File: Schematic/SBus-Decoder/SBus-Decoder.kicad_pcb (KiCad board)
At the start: 2 copper layers, 10 parts, among them J1 Conn_01x03_Male, J2 Conn_01x01_Male, J3 Conn_02x03_Odd_Even, U1 PIC16F18313-I_SN, U2 MCP1703A-3302_SOT23

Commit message: Initial pcb
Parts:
- moved C3 6.25 mm to (109.8, 105.8), turned to 180 degrees
- moved U1 5.15 mm to (115.5, 108.2)
- moved C2 5.03 mm to (115.2, 104.2)
- moved R1 4.27 mm to (117.8, 112.8), turned to 0 degrees
- moved J2 3.89 mm to (109.8, 113.2)
- moved U2 3.34 mm to (107.5, 108.8)
- moved C1 3.01 mm to (106.8, 112.8), turned to 270 degrees
- moved D1 2.36 mm to (114.0, 112.8), turned to 0 degrees
- moved J3 1.25 mm to (121.8, 106.5)
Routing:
- net VBUS: track 0.00 -> 29.1 mm
- net +3V3: track 0.00 -> 20.1 mm
- net GND: track 0.00 -> 16.0 mm, vias 0 -> 3
- net Net-(J1-Pad1): track 0.00 -> 12.7 mm
- net Net-(J3-Pad2): track 0.00 -> 7.25 mm
- net Net-(J3-Pad1): track 0.00 -> 4.06 mm
- net Net-(R1-Pad2): track 0.00 -> 2.77 mm
- net Net-(D1-Pad2): track 0.00 -> 2.14 mm
- net Net-(U1-Pad2): track 0.00 -> 1.27 mm
- added copper zone on B.Cu, net GND
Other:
- board outline added: 28.5 x 13.5 mm
- net class Power: trace_width 1 -> 0.5
- board text added: "S1"
- board text added: "S2"

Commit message: Schematic and pcb
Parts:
- added J4: TSW-104-08-G-T-RA, SamacSys_Parts:HDRRA12W64P254_3X4_1016X254X810P, F.Cu at (121.5, 106.0)
- J1: footprint Connector_Wire:SolderWire-0.75sqmm_1x03_P4.8mm_D1.25mm_OD2.3mm -> Connector_Wire:SolderWire-0.5sqmm_1x03_P4.6mm_D0.9mm_OD2.1mm
- J3: value Conn_02x03_Odd_Even -> Conn_01x01_Male; footprint Connector_PinHeader_2.54mm:PinHeader_2x03_P2.54mm_Horizontal -> Connector_PinHeader_2.54mm:PinHeader_1x01_P2.54mm_Vertical
- U1: value PIC16F18313-I_SN -> PIC18F04Q40-I_ST; footprint PIC16F18313:PIC16F18313-I&slash_SN -> PIC18F0xQ40:PIC18F04Q40-I&slash_ST
- moved J3 11.0 mm to (113.2, 113.5)
- moved D1 2.02 mm to (116.0, 113.0), turned to 270 degrees
- moved C2 1.03 mm to (114.2, 104.5)
- moved R1 0.56 mm to (118.2, 113.0), turned to 90 degrees
- moved U2 0.56 mm to (107.0, 109.0)
- moved C3 0.50 mm to (109.8, 106.2)
- moved J2 0.35 mm to (109.5, 113.5)
- moved J1 0.25 mm to (102.5, 104.2)
- moved U1 0.25 mm to (115.2, 108.2)
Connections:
- U1 pad 3: Net-(U1-Pad2) -> Net-(U1-Pad3)
- U1 pad 4: Net-(J1-Pad1) -> Net-(J3-Pad1)
- U1 pad 5: Net-(R1-Pad2) -> Net-(U1-Pad5)
- U1 pad 6: Net-(J3-Pad2) -> Net-(U1-Pad6)
- U1 pad 7: Net-(J3-Pad1) -> Net-(J1-Pad1)
- U1 pad 8: GND -> Net-(R1-Pad2)
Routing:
- net GND: track 16.0 -> 53.4 mm, vias 3 -> 4
- net VBUS: track 29.1 -> 40.2 mm
- net Net-(J3-Pad2): track 7.25 -> 0.00 mm
- net Net-(J4-Pad10): track 0.00 -> 5.99 mm
- net +3V3: track 20.1 -> 14.9 mm, vias 0 -> 1
- net Net-(J4-Pad7): track 0.00 -> 4.25 mm
- net Net-(J3-Pad1): track 4.06 -> 8.02 mm
- net Net-(J4-Pad1): track 0.00 -> 3.74 mm
- net Net-(J4-Pad4): track 0.00 -> 3.74 mm
- net Net-(U1-Pad2): track 1.27 -> 0.00 mm
- net Net-(R1-Pad2): track 2.77 -> 2.02 mm
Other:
- board size 28.5 x 13.5 mm -> 28.5 x 14.8 mm
- board text added: "*"
- board text added: "+"
- board text added: "-"
- board text added: "SBus Decoder V1.0 QES 2021"
- board text removed: "S1"
- board text removed: "S2"

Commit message: Single pcb layout complete
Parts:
- moved C1 72.3 mm to (56.8, 60.5)
- moved C2 72.3 mm to (64.2, 52.2)
- moved C3 72.3 mm to (59.8, 54.0)
- moved D1 72.3 mm to (66.0, 60.8)
- moved J2 72.3 mm to (59.5, 61.2)
- moved J3 72.3 mm to (63.2, 61.2)
- moved J4 72.3 mm to (71.5, 53.8)
- moved R1 72.3 mm to (68.2, 60.8)
- moved U1 72.3 mm to (65.2, 56.0)
- moved U2 72.3 mm to (57.0, 56.8)
- moved J1 71.9 mm to (52.5, 52.6)
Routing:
- net VBUS: track 40.2 -> 41.0 mm
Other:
- board size 28.5 x 14.8 mm -> 28.8 x 15.2 mm
- rule pad_to_mask_clearance: 0 -> 0.05

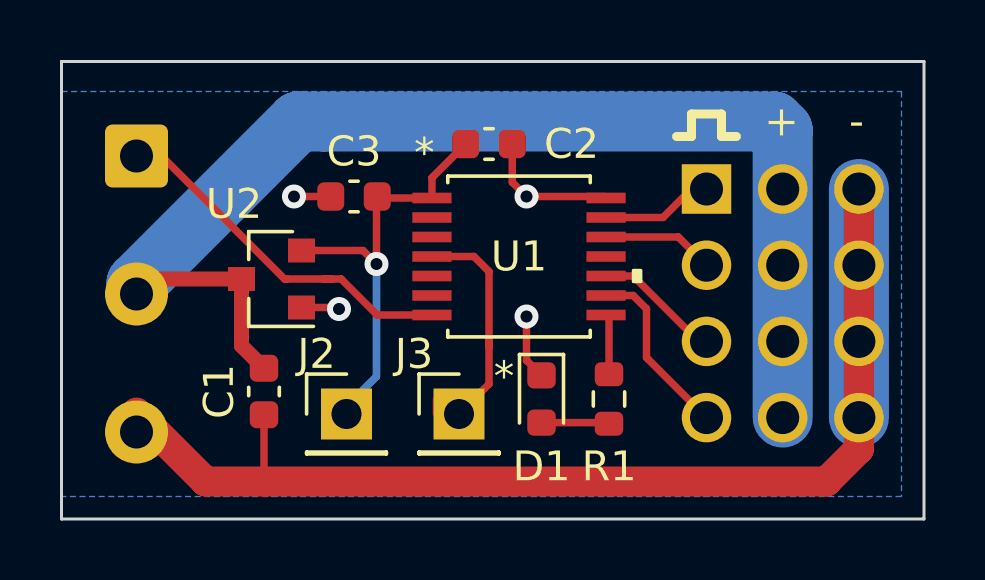
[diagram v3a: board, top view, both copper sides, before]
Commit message: Changed input connector footprint
Using a 2.54 pin header will allow for more flexibility for other uses (like a servo sequencer.)
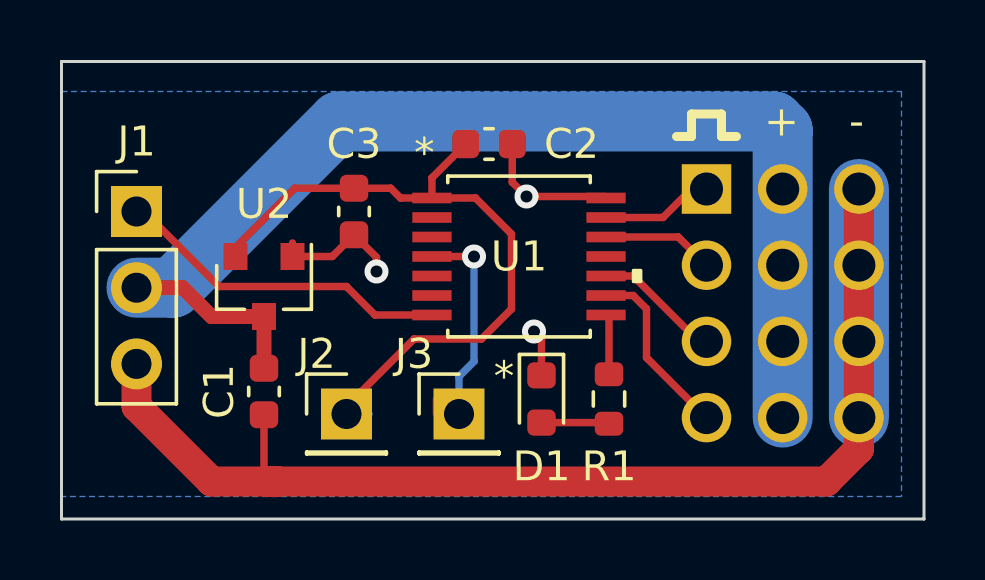
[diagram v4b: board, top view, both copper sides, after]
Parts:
- J1: footprint Connector_Wire:SolderWire-0.5sqmm_1x03_P4.6mm_D0.9mm_OD2.1mm -> Connector_PinHeader_2.54mm:PinHeader_1x03_P2.54mm_Vertical
- moved J1 1.85 mm to (52.5, 54.5), turned to 0 degrees
- moved C3 0.50 mm to (59.8, 54.5), turned to 270 degrees
- moved U2 0.35 mm to (56.8, 57.0), turned to 270 degrees
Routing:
- net +3V3: track 14.9 -> 23.8 mm, vias 1 -> 0
- net GND: track 53.4 -> 56.6 mm, vias 4 -> 3
- net Net-(J1-Pad1): track 12.8 -> 11.3 mm
- net Net-(J3-Pad1): track 8.02 -> 7.36 mm, vias 0 -> 1

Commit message: Better ICSP setup
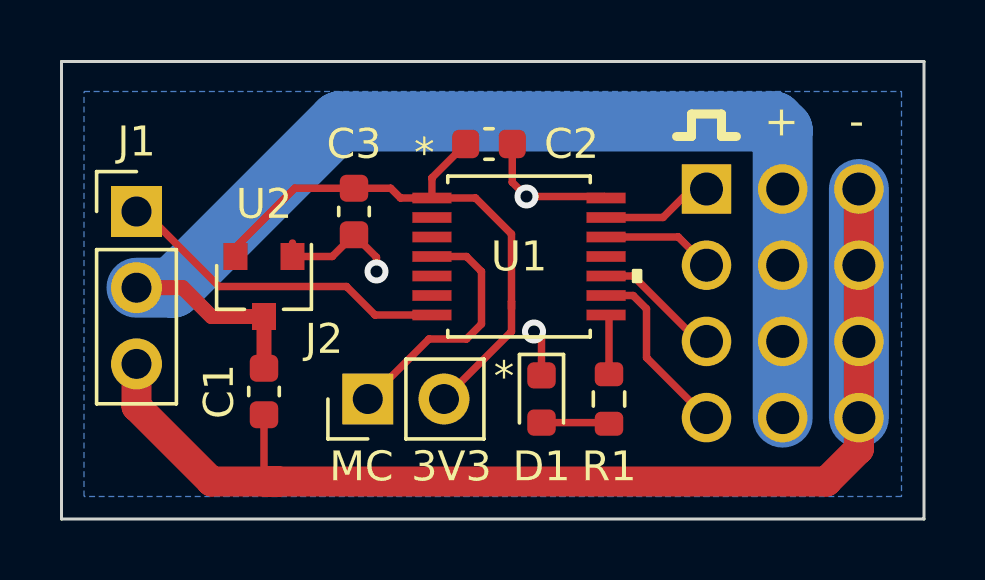
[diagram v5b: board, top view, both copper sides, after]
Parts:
- removed the J3 at (63.2, 61.2)
- C3: value 1 uF -> 2.2 uF
- J2: value Conn_01x01_Male -> Conn_01x02_Male; footprint Connector_PinHeader_2.54mm:PinHeader_1x01_P2.54mm_Vertical -> Connector_PinHeader_2.54mm:PinHeader_1x02_P2.54mm_Vertical
- moved J2 0.87 mm to (60.2, 60.8), turned to 90 degrees
- renumbered J4 to J3
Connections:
- J2 pad 1: +3V3 -> Net-(J2-Pad1)
- U1 pad 4: Net-(J3-Pad1) (its old number) -> Net-(J2-Pad1)
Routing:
- net Net-(J2-Pad1): track 0.00 -> 8.93 mm
- net Net-(J3-Pad1) (its old number): track 7.36 -> 0.00 mm, vias 1 -> 0
- net +3V3: track 23.8 -> 19.9 mm
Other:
- board text added: "3V3"
- board text added: "MC"

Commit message: Paneled and generated gerbers
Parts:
- added C1: 1 uF, Capacitor_SMD:C_0603_1608Metric, F.Cu at (112.2, 88.5)
- added C1: 1 uF, Capacitor_SMD:C_0603_1608Metric, F.Cu at (56.8, 102.5)
- added C1: 1 uF, Capacitor_SMD:C_0603_1608Metric, F.Cu at (56.8, 74.5)
- added C1: 1 uF, Capacitor_SMD:C_0603_1608Metric, F.Cu at (112.2, 102.5)
- added C1: 1 uF, Capacitor_SMD:C_0603_1608Metric, F.Cu at (112.2, 60.5)
- added C1: 1 uF, Capacitor_SMD:C_0603_1608Metric, F.Cu at (112.2, 74.5)
- added C1: 1 uF, Capacitor_SMD:C_0603_1608Metric, F.Cu at (84.5, 88.5)
- added C1: 1 uF, Capacitor_SMD:C_0603_1608Metric, F.Cu at (84.5, 102.5)
- added C1: 1 uF, Capacitor_SMD:C_0603_1608Metric, F.Cu at (84.5, 60.5)
- added C1: 1 uF, Capacitor_SMD:C_0603_1608Metric, F.Cu at (84.5, 74.5)
- added C1: 1 uF, Capacitor_SMD:C_0603_1608Metric, F.Cu at (56.8, 88.5)
- added C2: 0.1 uF, Capacitor_SMD:C_0603_1608Metric, F.Cu at (119.8, 80.2)
- added C2: 0.1 uF, Capacitor_SMD:C_0603_1608Metric, F.Cu at (64.2, 80.2)
- added C2: 0.1 uF, Capacitor_SMD:C_0603_1608Metric, F.Cu at (64.2, 66.2)
- added C2: 0.1 uF, Capacitor_SMD:C_0603_1608Metric, F.Cu at (119.8, 94.2)
- added C2: 0.1 uF, Capacitor_SMD:C_0603_1608Metric, F.Cu at (119.8, 52.2)
- added C2: 0.1 uF, Capacitor_SMD:C_0603_1608Metric, F.Cu at (119.8, 66.2)
- added C2: 0.1 uF, Capacitor_SMD:C_0603_1608Metric, F.Cu at (92.0, 94.2)
- added C2: 0.1 uF, Capacitor_SMD:C_0603_1608Metric, F.Cu at (92.0, 80.2)
- added C2: 0.1 uF, Capacitor_SMD:C_0603_1608Metric, F.Cu at (92.0, 66.2)
- added C2: 0.1 uF, Capacitor_SMD:C_0603_1608Metric, F.Cu at (92.0, 52.2)
- added C2: 0.1 uF, Capacitor_SMD:C_0603_1608Metric, F.Cu at (64.2, 94.2)
- added C3: 2.2 uF, Capacitor_SMD:C_0603_1608Metric, F.Cu at (115.2, 96.5)
- added C3: 2.2 uF, Capacitor_SMD:C_0603_1608Metric, F.Cu at (59.8, 96.5)
- added C3: 2.2 uF, Capacitor_SMD:C_0603_1608Metric, F.Cu at (59.8, 68.5)
- added C3: 2.2 uF, Capacitor_SMD:C_0603_1608Metric, F.Cu at (115.2, 82.5)
- added C3: 2.2 uF, Capacitor_SMD:C_0603_1608Metric, F.Cu at (115.2, 54.5)
- added C3: 2.2 uF, Capacitor_SMD:C_0603_1608Metric, F.Cu at (115.2, 68.5)
- added C3: 2.2 uF, Capacitor_SMD:C_0603_1608Metric, F.Cu at (87.5, 96.5)
- added C3: 2.2 uF, Capacitor_SMD:C_0603_1608Metric, F.Cu at (87.5, 82.5)
- added C3: 2.2 uF, Capacitor_SMD:C_0603_1608Metric, F.Cu at (87.5, 54.5)
- added C3: 2.2 uF, Capacitor_SMD:C_0603_1608Metric, F.Cu at (87.5, 68.5)
- added C3: 2.2 uF, Capacitor_SMD:C_0603_1608Metric, F.Cu at (59.8, 82.5)
- added D1: LED-Red, LED_SMD:LED_0603_1608Metric, F.Cu at (121.5, 102.8)
- added D1: LED-Red, LED_SMD:LED_0603_1608Metric, F.Cu at (66.0, 102.8)
- added D1: LED-Red, LED_SMD:LED_0603_1608Metric, F.Cu at (66.0, 74.8)
- added D1: LED-Red, LED_SMD:LED_0603_1608Metric, F.Cu at (121.5, 74.8)
- added D1: LED-Red, LED_SMD:LED_0603_1608Metric, F.Cu at (121.5, 60.8)
- added D1: LED-Red, LED_SMD:LED_0603_1608Metric, F.Cu at (121.5, 88.8)
- added D1: LED-Red, LED_SMD:LED_0603_1608Metric, F.Cu at (93.8, 60.8)
- added D1: LED-Red, LED_SMD:LED_0603_1608Metric, F.Cu at (93.8, 102.8)
- added D1: LED-Red, LED_SMD:LED_0603_1608Metric, F.Cu at (93.8, 74.8)
- added D1: LED-Red, LED_SMD:LED_0603_1608Metric, F.Cu at (93.8, 88.8)
- added D1: LED-Red, LED_SMD:LED_0603_1608Metric, F.Cu at (66.0, 88.8)
- added J1: Conn_01x03_Male, Connector_PinHeader_2.54mm:PinHeader_1x03_P2.54mm_Vertical, F.Cu at (108.0, 68.5)
- added J1: Conn_01x03_Male, Connector_PinHeader_2.54mm:PinHeader_1x03_P2.54mm_Vertical, F.Cu at (52.5, 96.5)
- added J1: Conn_01x03_Male, Connector_PinHeader_2.54mm:PinHeader_1x03_P2.54mm_Vertical, F.Cu at (52.5, 68.5)
- added J1: Conn_01x03_Male, Connector_PinHeader_2.54mm:PinHeader_1x03_P2.54mm_Vertical, F.Cu at (108.0, 54.5)
- added J1: Conn_01x03_Male, Connector_PinHeader_2.54mm:PinHeader_1x03_P2.54mm_Vertical, F.Cu at (108.0, 82.5)
- added J1: Conn_01x03_Male, Connector_PinHeader_2.54mm:PinHeader_1x03_P2.54mm_Vertical, F.Cu at (108.0, 96.5)
- added J1: Conn_01x03_Male, Connector_PinHeader_2.54mm:PinHeader_1x03_P2.54mm_Vertical, F.Cu at (80.2, 54.5)
- added J1: Conn_01x03_Male, Connector_PinHeader_2.54mm:PinHeader_1x03_P2.54mm_Vertical, F.Cu at (80.2, 68.5)
- added J1: Conn_01x03_Male, Connector_PinHeader_2.54mm:PinHeader_1x03_P2.54mm_Vertical, F.Cu at (80.2, 82.5)
- added J1: Conn_01x03_Male, Connector_PinHeader_2.54mm:PinHeader_1x03_P2.54mm_Vertical, F.Cu at (80.2, 96.5)
- added J1: Conn_01x03_Male, Connector_PinHeader_2.54mm:PinHeader_1x03_P2.54mm_Vertical, F.Cu at (52.5, 82.5)
- added J2: Conn_01x02_Male, Connector_PinHeader_2.54mm:PinHeader_1x02_P2.54mm_Vertical, F.Cu at (115.7, 102.8)
- added J2: Conn_01x02_Male, Connector_PinHeader_2.54mm:PinHeader_1x02_P2.54mm_Vertical, F.Cu at (60.2, 88.8)
- added J2: Conn_01x02_Male, Connector_PinHeader_2.54mm:PinHeader_1x02_P2.54mm_Vertical, F.Cu at (60.2, 74.8)
- added J2: Conn_01x02_Male, Connector_PinHeader_2.54mm:PinHeader_1x02_P2.54mm_Vertical, F.Cu at (115.7, 88.8)
- added J2: Conn_01x02_Male, Connector_PinHeader_2.54mm:PinHeader_1x02_P2.54mm_Vertical, F.Cu at (115.7, 60.8)
- added J2: Conn_01x02_Male, Connector_PinHeader_2.54mm:PinHeader_1x02_P2.54mm_Vertical, F.Cu at (115.7, 74.8)
- added J2: Conn_01x02_Male, Connector_PinHeader_2.54mm:PinHeader_1x02_P2.54mm_Vertical, F.Cu at (88.0, 88.8)
- added J2: Conn_01x02_Male, Connector_PinHeader_2.54mm:PinHeader_1x02_P2.54mm_Vertical, F.Cu at (88.0, 102.8)
- added J2: Conn_01x02_Male, Connector_PinHeader_2.54mm:PinHeader_1x02_P2.54mm_Vertical, F.Cu at (88.0, 74.8)
- added J2: Conn_01x02_Male, Connector_PinHeader_2.54mm:PinHeader_1x02_P2.54mm_Vertical, F.Cu at (88.0, 60.8)
- added J2: Conn_01x02_Male, Connector_PinHeader_2.54mm:PinHeader_1x02_P2.54mm_Vertical, F.Cu at (60.2, 102.8)
- added J3: TSW-104-08-G-T-RA, SamacSys_Parts:HDRRA12W64P254_3X4_1016X254X810P, F.Cu at (127.0, 67.8)
- added J3: TSW-104-08-G-T-RA, SamacSys_Parts:HDRRA12W64P254_3X4_1016X254X810P, F.Cu at (71.5, 95.8)
- added J3: TSW-104-08-G-T-RA, SamacSys_Parts:HDRRA12W64P254_3X4_1016X254X810P, F.Cu at (71.5, 67.8)
- added J3: TSW-104-08-G-T-RA, SamacSys_Parts:HDRRA12W64P254_3X4_1016X254X810P, F.Cu at (127.0, 95.8)
- added J3: TSW-104-08-G-T-RA, SamacSys_Parts:HDRRA12W64P254_3X4_1016X254X810P, F.Cu at (127.0, 53.8)
- added J3: TSW-104-08-G-T-RA, SamacSys_Parts:HDRRA12W64P254_3X4_1016X254X810P, F.Cu at (127.0, 81.8)
- added J3: TSW-104-08-G-T-RA, SamacSys_Parts:HDRRA12W64P254_3X4_1016X254X810P, F.Cu at (99.2, 53.8)
- added J3: TSW-104-08-G-T-RA, SamacSys_Parts:HDRRA12W64P254_3X4_1016X254X810P, F.Cu at (99.2, 95.8)
- added J3: TSW-104-08-G-T-RA, SamacSys_Parts:HDRRA12W64P254_3X4_1016X254X810P, F.Cu at (99.2, 67.8)
- added J3: TSW-104-08-G-T-RA, SamacSys_Parts:HDRRA12W64P254_3X4_1016X254X810P, F.Cu at (99.2, 81.8)
- added J3: TSW-104-08-G-T-RA, SamacSys_Parts:HDRRA12W64P254_3X4_1016X254X810P, F.Cu at (71.5, 81.8)
- added R1: 220, Resistor_SMD:R_0603_1608Metric, F.Cu at (123.8, 74.8)
- added R1: 220, Resistor_SMD:R_0603_1608Metric, F.Cu at (68.2, 102.8)
- added R1: 220, Resistor_SMD:R_0603_1608Metric, F.Cu at (68.2, 74.8)
- added R1: 220, Resistor_SMD:R_0603_1608Metric, F.Cu at (123.8, 60.8)
- added R1: 220, Resistor_SMD:R_0603_1608Metric, F.Cu at (123.8, 102.8)
- added R1: 220, Resistor_SMD:R_0603_1608Metric, F.Cu at (123.8, 88.8)
- added R1: 220, Resistor_SMD:R_0603_1608Metric, F.Cu at (96.0, 60.8)
- added R1: 220, Resistor_SMD:R_0603_1608Metric, F.Cu at (96.0, 74.8)
- added R1: 220, Resistor_SMD:R_0603_1608Metric, F.Cu at (96.0, 88.8)
- added R1: 220, Resistor_SMD:R_0603_1608Metric, F.Cu at (96.0, 102.8)
- added R1: 220, Resistor_SMD:R_0603_1608Metric, F.Cu at (68.2, 88.8)
- added U1: PIC18F04Q40-I_ST, PIC18F0xQ40:PIC18F04Q40-I&slash_ST, F.Cu at (120.8, 98.0)
- added U1: PIC18F04Q40-I_ST, PIC18F0xQ40:PIC18F04Q40-I&slash_ST, F.Cu at (65.2, 84.0)
- added U1: PIC18F04Q40-I_ST, PIC18F0xQ40:PIC18F04Q40-I&slash_ST, F.Cu at (65.2, 70.0)
- added U1: PIC18F04Q40-I_ST, PIC18F0xQ40:PIC18F04Q40-I&slash_ST, F.Cu at (120.8, 84.0)
- added U1: PIC18F04Q40-I_ST, PIC18F0xQ40:PIC18F04Q40-I&slash_ST, F.Cu at (120.8, 56.0)
- added U1: PIC18F04Q40-I_ST, PIC18F0xQ40:PIC18F04Q40-I&slash_ST, F.Cu at (120.8, 70.0)
- added U1: PIC18F04Q40-I_ST, PIC18F0xQ40:PIC18F04Q40-I&slash_ST, F.Cu at (93.0, 98.0)
- added U1: PIC18F04Q40-I_ST, PIC18F0xQ40:PIC18F04Q40-I&slash_ST, F.Cu at (93.0, 84.0)
- added U1: PIC18F04Q40-I_ST, PIC18F0xQ40:PIC18F04Q40-I&slash_ST, F.Cu at (93.0, 70.0)
- added U1: PIC18F04Q40-I_ST, PIC18F0xQ40:PIC18F04Q40-I&slash_ST, F.Cu at (93.0, 56.0)
- added U1: PIC18F04Q40-I_ST, PIC18F0xQ40:PIC18F04Q40-I&slash_ST, F.Cu at (65.2, 98.0)
- added U2: MCP1703A-3302_SOT23, Package_TO_SOT_SMD:SOT-23, F.Cu at (112.2, 85.0)
- added U2: MCP1703A-3302_SOT23, Package_TO_SOT_SMD:SOT-23, F.Cu at (56.8, 85.0)
- added U2: MCP1703A-3302_SOT23, Package_TO_SOT_SMD:SOT-23, F.Cu at (56.8, 71.0)
- added U2: MCP1703A-3302_SOT23, Package_TO_SOT_SMD:SOT-23, F.Cu at (112.2, 99.0)
- added U2: MCP1703A-3302_SOT23, Package_TO_SOT_SMD:SOT-23, F.Cu at (112.2, 57.0)
- added U2: MCP1703A-3302_SOT23, Package_TO_SOT_SMD:SOT-23, F.Cu at (112.2, 71.0)
- added U2: MCP1703A-3302_SOT23, Package_TO_SOT_SMD:SOT-23, F.Cu at (84.5, 85.0)
- added U2: MCP1703A-3302_SOT23, Package_TO_SOT_SMD:SOT-23, F.Cu at (84.5, 99.0)
- added U2: MCP1703A-3302_SOT23, Package_TO_SOT_SMD:SOT-23, F.Cu at (84.5, 71.0)
- added U2: MCP1703A-3302_SOT23, Package_TO_SOT_SMD:SOT-23, F.Cu at (84.5, 57.0)
- added U2: MCP1703A-3302_SOT23, Package_TO_SOT_SMD:SOT-23, F.Cu at (56.8, 99.0)
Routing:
- net GND: track 56.6 -> 679.5 mm, vias 3 -> 36
- net VBUS: track 40.6 -> 487.4 mm
- net +3V3: track 19.9 -> 238.8 mm
- net Net-(J1-Pad1): track 11.3 -> 135.3 mm
- net Net-(J2-Pad1): track 8.93 -> 107.2 mm
- net Net-(J3-Pad10): track 5.99 -> 71.8 mm
- net Net-(J3-Pad7): track 4.25 -> 51.0 mm
- net Net-(J3-Pad1): track 3.74 -> 44.9 mm
- net Net-(J3-Pad4): track 3.74 -> 44.8 mm
- net Net-(D1-Pad2): track 2.27 -> 27.2 mm
- net Net-(R1-Pad2): track 2.02 -> 24.2 mm
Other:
- board size 28.8 x 15.2 mm -> 84 x 56.5 mm
- board text added: "JLCJLCJLCJLC"

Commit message: Converted to KiCad 6
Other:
- net class Default removed
- net class Power removed
